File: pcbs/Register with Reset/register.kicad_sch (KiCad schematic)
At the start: 27 parts, among them U201 74HC245, U202 74HCT574, U203 74HC245

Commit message: Adding design rules
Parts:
- renumbered D201 to D301, D202 to D302, D203 to D303, D204 to D304, D205 to D305, D206 to D306, D207 to D307, D208 to D308, R201 to R301, R202 to R302, R203 to R303, R204 to R304, R205 to R305, R206 to R306, R207 to R307, R208 to R308, R209 to R309, R210 to R310, R211 to R311, R212 to R312, R213 to R313, R214 to R314, R215 to R315, R216 to R316, U201 to U301, U202 to U302, U203 to U303
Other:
- title: (none) -> 16-bit Register with Reset
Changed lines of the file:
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@@
 	(generator_version "8.0")
 	(paper "A4")
+	(title_block
+		(title "16-bit Register with Reset")
+		(rev "0")
+	)
 	(junction
 		(at 207.01 57.15)
@@
 	(label "Out4"
 		(at 264.16 52.07 0)
+		(fields_autoplaced yes)
 		(effects
 			(font
@@
 	(label "Out0"
 		(at 264.16 41.91 0)
+		(fields_autoplaced yes)
 		(effects
 			(font
@@
 	(label "In2"
 		(at 27.94 46.99 0)
+		(fields_autoplaced yes)
 		(effects
 			(font
@@
 	(label "Out6"
 		(at 264.16 57.15 0)
+		(fields_autoplaced yes)
 		(effects
 			(font
@@
 	(label "In5"
 		(at 27.94 54.61 0)
+		(fields_autoplaced yes)
 		(effects
 			(font
@@
 	(label "In7"
 		(at 27.94 59.69 0)
+		(fields_autoplaced yes)
 		(effects
 			(font
@@
 	(label "In6"
 		(at 27.94 57.15 0)
+		(fields_autoplaced yes)
 		(effects
 			(font
@@
 	(label "Out2"
 		(at 264.16 46.99 0)
+		(fields_autoplaced yes)
 		(effects
 			(font
@@
 	(label "In0"
 		(at 27.94 41.91 0)
+		(fields_autoplaced yes)
 		(effects
 			(font
@@
 	(label "Out7"
 		(at 264.16 59.69 0)
+		(fields_autoplaced yes)
 		(effects
 			(font
@@
 	(label "In1"
 		(at 27.94 44.45 0)
+		(fields_autoplaced yes)
 		(effects
 			(font
@@
 	(label "Out5"
 		(at 264.16 54.61 0)
+		(fields_autoplaced yes)
 		(effects
 			(font
@@
 	(label "Out3"
 		(at 264.16 49.53 0)
+		(fields_autoplaced yes)
 		(effects
 			(font
@@
 	(label "Out1"
 		(at 264.16 44.45 0)
+		(fields_autoplaced yes)
 		(effects
 			(font
@@
 	(label "In3"
 		(at 27.94 49.53 0)
+		(fields_autoplaced yes)
 		(effects
 			(font
@@
 	(label "In4"
 		(at 27.94 52.07 0)
+		(fields_autoplaced yes)
 		(effects
 			(font
@@
 		(dnp no)
 		(fields_autoplaced yes)
-		(property "Reference" "R214"
+		(property "Reference" "R314"
 			(at 199.39 93.9799 0)
 			(effects
@@
 		(dnp no)
 		(fields_autoplaced yes)
-		(property "Reference" "U202"
+		(property "Reference" "U302"
 			(at 134.2741 34.29 0)
 			(effects
@@
 		(dnp no)
 		(fields_autoplaced yes)
-		(property "Reference" "R204"
+		(property "Reference" "R304"
 			(at 80.01 67.3099 0)
 			(effects
@@
 		(dnp no)
 		(fields_autoplaced yes)
-		(property "Reference" "D203"
+		(property "Reference" "D303"
 			(at 170.18 80.3274 90)
 			(effects
@@
 		(dnp no)
 		(fields_autoplaced yes)
-		(property "Reference" "#PWR0212"
+		(property "Reference" "#PWR0312"
 			(at 251.46 87.63 0)
 			(effects
@@
 		(dnp no)
 		(fields_autoplaced yes)
-		(property "Reference" "#PWR0211"
+		(property "Reference" "#PWR0311"
 			(at 251.46 33.02 0)
 			(effects
@@
 		(dnp no)
 		(fields_autoplaced yes)
-		(property "Reference" "R216"
+		(property "Reference" "R316"
 			(at 219.71 93.9799 0)
 			(effects
@@
 		(dnp no)
 		(fields_autoplaced yes)
-		(property "Reference" "D205"
+		(property "Reference" "D305"
 			(at 190.5 80.3274 90)
 			(effects
@@
 		(dnp no)
 		(fields_autoplaced yes)
-		(property "Reference" "R206"
+		(property "Reference" "R306"
 			(at 88.9 67.3099 0)
 			(effects
@@
 		(dnp no)
 		(fields_autoplaced yes)
-		(property "Reference" "#PWR0203"
+		(property "Reference" "#PWR0303"
 			(at 50.8 87.63 0)
 			(effects
@@
 		(dnp no)
 		(fields_autoplaced yes)
-		(property "Reference" "R210"
+		(property "Reference" "R310"
 			(at 158.75 93.9799 0)
 			(effects
@@
 		(dnp no)
 		(fields_autoplaced yes)
-		(property "Reference" "#PWR0208"
+		(property "Reference" "#PWR0308"
 			(at 132.08 87.63 0)
 			(effects
@@
 		(dnp no)
 		(fields_autoplaced yes)
-		(property "Reference" "R209"
+		(property "Reference" "R309"
 			(at 149.86 93.9799 0)
 			(effects
@@
 		(dnp no)
 		(fields_autoplaced yes)
-		(property "Reference" "#PWR0205"
+		(property "Reference" "#PWR0305"
 			(at 68.58 85.09 0)
 			(effects
@@
 		(dnp no)
 		(fields_autoplaced yes)
-		(property "Reference" "R211"
+		(property "Reference" "R311"
 			(at 168.91 93.9799 0)
 			(effects
@@
 		(dnp no)
 		(fields_autoplaced yes)
-		(property "Reference" "R202"
+		(property "Reference" "R302"
 			(at 71.12 67.3099 0)
 			(effects
@@
 		(dnp no)
 		(fields_autoplaced yes)
-		(property "Reference" "R203"
+		(property "Reference" "R303"
 			(at 80.01 33.0199 0)
 			(effects
@@
 		(dnp no)
 		(fields_autoplaced yes)
-		(property "Reference" "D204"
+		(property "Reference" "D304"
 			(at 180.34 80.3274 90)
 			(effects
@@
 		(dnp no)
 		(fields_autoplaced yes)
-		(property "Reference" "#PWR0202"
+		(property "Reference" "#PWR0302"
 			(at 50.8 34.29 0)
 			(effects
@@
 		(dnp no)
 		(fields_autoplaced yes)
-		(property "Reference" "#PWR0207"
+		(property "Reference" "#PWR0307"
 			(at 132.08 35.56 0)
 			(effects
@@
 		(dnp no)
 		(fields_autoplaced yes)
-		(property "Reference" "R212"
+		(property "Reference" "R312"
 			(at 179.07 93.9799 0)
 			(effects
@@
 		(dnp no)
 		(fields_autoplaced yes)
-		(property "Reference" "R207"
+		(property "Reference" "R307"
 			(at 97.79 33.0199 0)
 			(effects
@@
 		(dnp no)
 		(fields_autoplaced yes)
-		(property "Reference" "#PWR0206"
+		(property "Reference" "#PWR0306"
 			(at 106.68 67.31 0)
 			(effects
@@
 		(dnp no)
 		(fields_autoplaced yes)
-		(property "Reference" "R213"
+		(property "Reference" "R313"
 			(at 189.23 93.9799 0)
 			(effects
@@
 		(dnp no)
 		(fields_autoplaced yes)
-		(property "Reference" "U203"
+		(property "Reference" "U303"
 			(at 253.6541 34.29 0)
 			(effects
@@
 		(dnp no)
 		(fields_autoplaced yes)
-		(property "Reference" "R215"
+		(property "Reference" "R315"
 			(at 209.55 93.9799 0)
 			(effects
@@
 		(dnp no)
 		(fields_autoplaced yes)
-		(property "Reference" "R205"
+		(property "Reference" "R305"
 			(at 88.9 33.0199 0)
 			(effects
@@
 		(dnp no)
 		(fields_autoplaced yes)
-		(property "Reference" "#PWR0210"
+		(property "Reference" "#PWR0310"
 			(at 236.22 64.77 0)
 			(effects
@@
 		(dnp no)
 		(fields_autoplaced yes)
-		(property "Reference" "D206"
+		(property "Reference" "D306"
 			(at 200.66 80.3274 90)
 			(effects
@@
 		(dnp no)
 		(fields_autoplaced yes)
-		(property "Reference" "#PWR0204"
+		(property "Reference" "#PWR0304"
 			(at 68.58 19.05 0)
 			(effects
@@
 		(dnp no)
 		(fields_autoplaced yes)
-		(property "Reference" "R201"
+		(property "Reference" "R301"
 			(at 71.12 33.0199 0)
 			(effects
@@
 		(dnp no)
 		(fields_autoplaced yes)
-		(property "Reference" "#PWR0201"
+		(property "Reference" "#PWR0301"
 			(at 35.56 64.77 0)
 			(effects
@@
 		(dnp no)
 		(fields_autoplaced yes)
-		(property "Reference" "#PWR0209"
+		(property "Reference" "#PWR0309"
 			(at 147.32 110.49 0)
 			(effects
@@
 		(dnp no)
 		(fields_autoplaced yes)
-		(property "Reference" "D208"
+		(property "Reference" "D308"
 			(at 220.98 80.3274 90)
 			(effects
@@
 		(dnp no)
 		(fields_autoplaced yes)
-		(property "Reference" "D207"
+		(property "Reference" "D307"
 			(at 210.82 80.3274 90)
 			(effects
@@
 		(dnp no)
 		(fields_autoplaced yes)
-		(property "Reference" "D202"
+		(property "Reference" "D302"
 			(at 160.02 80.3274 90)
 			(effects
@@
 		(dnp no)
 		(fields_autoplaced yes)
-		(property "Reference" "U201"
+		(property "Reference" "U301"
 			(at 52.9941 34.29 0)
 			(effects
@@
 		(dnp no)
 		(fields_autoplaced yes)
-		(property "Reference" "R208"
+		(property "Reference" "R308"
 			(at 97.79 67.3099 0)
 			(effects
@@
 		(dnp no)
 		(fields_autoplaced yes)
-		(property "Reference" "D201"
+		(property "Reference" "D301"
 			(at 151.13 80.3274 90)
 			(effects

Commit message: Routing the actual registers
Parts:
- added C201: C, Capacitor_SMD:C_0603_1608Metric, symbol Device:C
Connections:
- net +5V: now also C201.1; no longer U303.1 (A->B)
- net GND: now also U303.1 (A->B), C201.2
- net Out0: now also U303.9 (A7); no longer U303.18 (B0)
- net Out1: now also U303.8 (A6); no longer U303.17 (B1)
- net Out2: now also U303.7 (A5); no longer U303.16 (B2)
- net Out3: now also U303.6 (A4); no longer U303.15 (B3)
- net Out4: now also U303.5 (A3); no longer U303.14 (B4)
- net Out5: now also U303.4 (A2); no longer U303.13 (B5)
- net Out6: now also U303.3 (A1); no longer U303.12 (B6)
- net Out7: now also U303.2 (A0); no longer U303.11 (B7)
- net RegClk: now reaches U302.11 (Cp)
- net at D308.2 (A), U302.12 (Q7): now also U303.18 (B0); no longer U303.9 (A7)
- net at D307.2 (A), U302.13 (Q6): now also U303.17 (B1); no longer U303.8 (A6)
- net at D306.2 (A), U302.14 (Q5): now also U303.16 (B2); no longer U303.7 (A5)
- net at D305.2 (A), U302.15 (Q4): now also U303.15 (B3); no longer U303.6 (A4)
- net at D304.2 (A), U302.16 (Q3): now also U303.14 (B4); no longer U303.5 (A3)
- net at D303.2 (A), U302.17 (Q2): now also U303.13 (B5); no longer U303.4 (A2)
- net at D302.2 (A), U302.18 (Q1): now also U303.12 (B6); no longer U303.3 (A1)
- net at D301.2 (A), U302.19 (Q0): now also U303.11 (B7); no longer U303.2 (A0)
- net at U301.17 (B1), U302.3 (D1): now also R302.1; no longer R303.2
- net at U301.16 (B2), U302.4 (D2): now also R303.2; no longer R305.2
- net at U301.15 (B3), U302.5 (D3): now also R304.1; no longer R307.2
- net at U301.14 (B4), U302.6 (D4): now also R305.2; no longer R302.1
- net at U301.13 (B5), U302.7 (D5): now also R306.1; no longer R304.1
- net at U301.12 (B6), U302.8 (D6): now also R307.2; no longer R306.1
- net ~{OE}: now reaches U303.19 (CE)
- net ~{ZeroInput}: now reaches U301.19 (CE)
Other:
- moved on the sheet: U303

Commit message: Working on reset logic and some routing
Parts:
- renumbered C201 to C301
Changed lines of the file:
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@@
 		(dnp no)
 		(fields_autoplaced yes)
-		(property "Reference" "C201"
+		(property "Reference" "C301"
 			(at 132.08 132.0799 0)
 			(effects
@@
 		(dnp no)
 		(fields_autoplaced yes)
-		(property "Reference" "#PWR0213"
+		(property "Reference" "#PWR0313"
 			(at 128.27 146.05 0)
 			(effects
@@
 		(dnp no)
 		(fields_autoplaced yes)
-		(property "Reference" "#PWR0214"
+		(property "Reference" "#PWR0314"
 			(at 128.27 129.54 0)
 			(effects

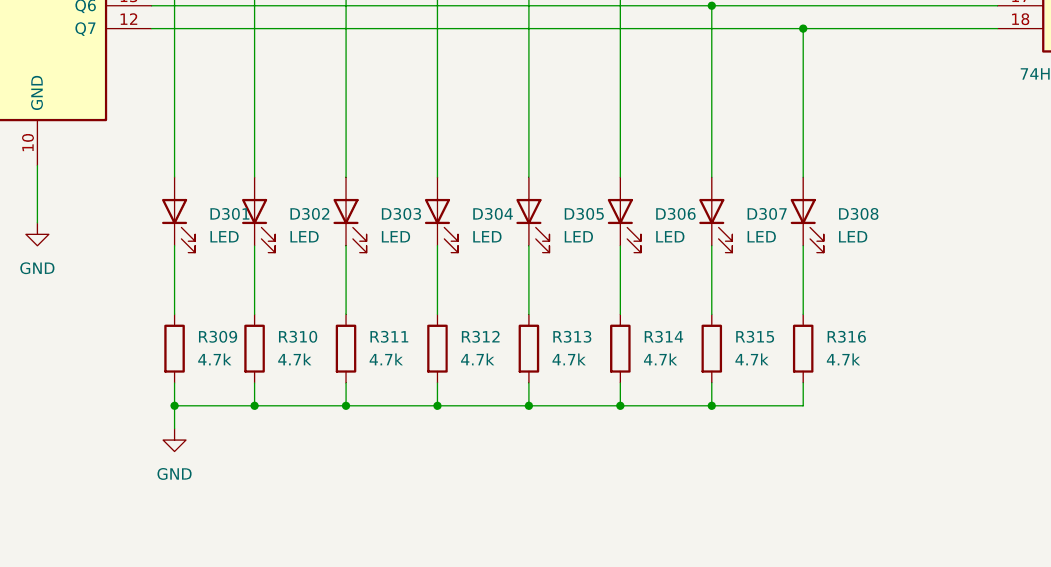
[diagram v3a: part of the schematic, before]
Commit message: First draft of whole board
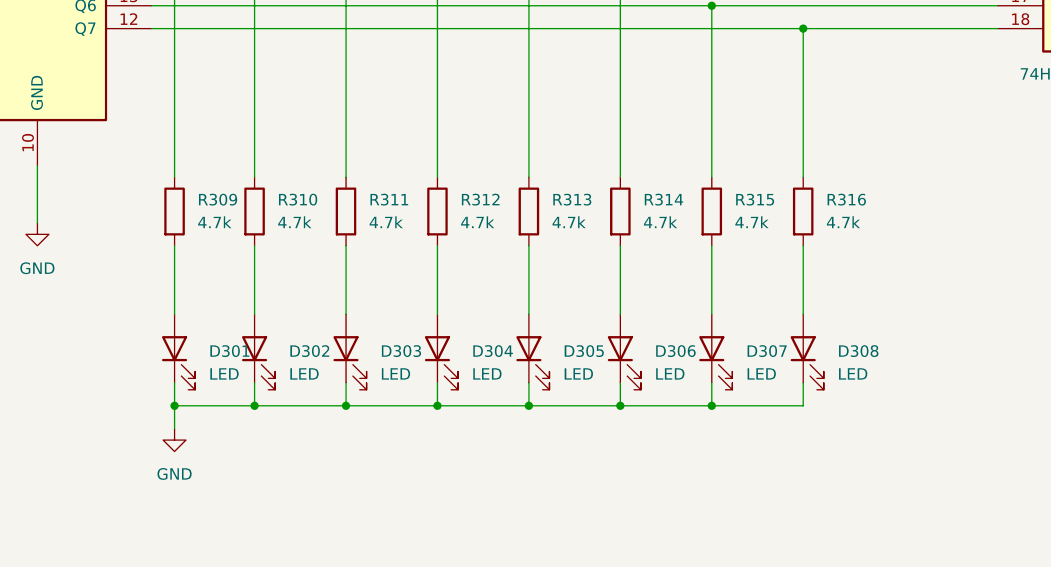
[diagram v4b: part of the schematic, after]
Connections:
- net GND: now also D301.1 (K), D302.1 (K), D303.1 (K), D304.1 (K), D305.1 (K), D306.1 (K), D307.1 (K), D308.1 (K); no longer R309.2, R310.2, R311.2, R312.2, R313.2, R314.2, R315.2, R316.2
- net at R314.1: now also U302.14 (Q5), U303.16 (B2); no longer D306.1 (K)
- net at U302.12 (Q7), U303.18 (B0): now also R316.1; no longer D308.2 (A)
- net at U302.13 (Q6), U303.17 (B1): now also R315.1; no longer D307.2 (A)
- net at U302.15 (Q4), U303.15 (B3): now also R313.1; no longer D305.2 (A)
- net at U302.16 (Q3), U303.14 (B4): now also R312.1; no longer D304.2 (A)
- net at U302.17 (Q2), U303.13 (B5): now also R311.1; no longer D303.2 (A)
- net at U302.18 (Q1), U303.12 (B6): now also R310.1; no longer D302.2 (A)
- net at U302.19 (Q0), U303.11 (B7): now also R309.1; no longer D301.2 (A)
- new net: D306.2 (A), R314.2
- new net: D303.2 (A), R311.2
- new net: D308.2 (A), R316.2
- new net: D305.2 (A), R313.2
- new net: D302.2 (A), R310.2
- new net: D301.2 (A), R309.2
- new net: D304.2 (A), R312.2
- new net: D307.2 (A), R315.2
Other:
- moved on the sheet: D301, D302, D303, D304, D305, D306, D307, D308, R309, R310, R311, R312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

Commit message: Fix the reset logic....
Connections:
- net ~{ZeroInput} renamed ZeroInput
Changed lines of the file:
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@@
 		)
 	)
-	(hierarchical_label "~{ZeroInput}"
+	(hierarchical_label "ZeroInput"
 		(shape input)
 		(at 26.67 67.31 180)

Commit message: Get buses routed
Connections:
- net Out0: now also U303.2 (A0); no longer U303.9 (A7)
- net Out1: now also U303.3 (A1); no longer U303.8 (A6)
- net Out2: now also U303.4 (A2); no longer U303.7 (A5)
- net Out3: now also U303.5 (A3); no longer U303.6 (A4)
- net Out4: now also U303.6 (A4); no longer U303.5 (A3)
- net Out5: now also U303.7 (A5); no longer U303.4 (A2)
- net Out6: now also U303.8 (A6); no longer U303.3 (A1)
- net Out7: now also U303.9 (A7); no longer U303.2 (A0)
- net at R314.1, U302.14 (Q5): now also U303.13 (B5); no longer U303.16 (B2)
- net at R316.1, U302.12 (Q7): now also U303.11 (B7); no longer U303.18 (B0)
- net at R315.1, U302.13 (Q6): now also U303.12 (B6); no longer U303.17 (B1)
- net at R313.1, U302.15 (Q4): now also U303.14 (B4); no longer U303.15 (B3)
- net at R312.1, U302.16 (Q3): now also U303.15 (B3); no longer U303.14 (B4)
- net at R311.1, U302.17 (Q2): now also U303.16 (B2); no longer U303.13 (B5)
- net at R310.1, U302.18 (Q1): now also U303.17 (B1); no longer U303.12 (B6)
- net at R309.1, U302.19 (Q0): now also U303.18 (B0); no longer U303.11 (B7)
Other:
- moved on the sheet: U303
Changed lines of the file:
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@@
 	(wire
 		(pts
-			(xy 264.16 34.29) (xy 269.24 34.29)
+			(xy 264.16 67.31) (xy 269.24 67.31)
 		)
 		(stroke
@@
 	(wire
 		(pts
-			(xy 251.46 22.86) (xy 251.46 26.67)
+			(xy 251.46 78.74) (xy 251.46 74.93)
 		)
 		(stroke
@@
 	(wire
 		(pts
-			(xy 251.46 67.31) (xy 251.46 71.12)
+			(xy 251.46 34.29) (xy 251.46 30.48)
 		)
 		(stroke
@@
 	(wire
 		(pts
-			(xy 264.16 36.83) (xy 267.97 36.83)
+			(xy 264.16 64.77) (xy 267.97 64.77)
 		)
 		(stroke
@@
 	(hierarchical_label "~{OE}"
 		(shape input)
-		(at 269.24 34.29 0)
+		(at 269.24 67.31 0)
 		(fields_autoplaced yes)
 		(effects
@@
 	(symbol
 		(lib_id "power:GND")
-		(at 251.46 22.86 180)
+		(at 251.46 78.74 0)
 		(unit 1)
 		(exclude_from_sim no)
@@
 		(fields_autoplaced yes)
 		(property "Reference" "#PWR0312"
-			(at 251.46 16.51 0)
+			(at 251.46 85.09 0)
 			(effects
 				(font
@@
 		)
 		(property "Value" "GND"
-			(at 251.46 17.78 0)
+			(at 251.46 83.82 0)
 			(effects
 				(font
@@
 		)
 		(property "Footprint" ""
-			(at 251.46 22.86 0)
+			(at 251.46 78.74 0)
 			(effects
 				(font
@@
 		)
 		(property "Datasheet" ""
-			(at 251.46 22.86 0)
+			(at 251.46 78.74 0)
 			(effects
 				(font
@@
 		)
 		(property "Description" "Power symbol creates a global label with name \"GND\" , ground"
-			(at 251.46 22.86 0)
+			(at 251.46 78.74 0)
 			(effects
 				(font
@@
 	(symbol
 		(lib_id "power:+5V")
-		(at 251.46 71.12 180)
+		(at 251.46 30.48 0)
 		(unit 1)
 		(exclude_from_sim no)
@@
 		(fields_autoplaced yes)
 		(property "Reference" "#PWR0311"
-			(at 251.46 67.31 0)
+			(at 251.46 34.29 0)
 			(effects
 				(font
@@
 		)
 		(property "Value" "+5V"
-			(at 251.46 76.2 0)
+			(at 251.46 25.4 0)
 			(effects
 				(font
@@
 		)
 		(property "Footprint" ""
-			(at 251.46 71.12 0)
+			(at 251.46 30.48 0)
 			(effects
 				(font
@@
 		)
 		(property "Datasheet" ""
-			(at 251.46 71.12 0)
+			(at 251.46 30.48 0)
 			(effects
 				(font
@@
 		)
 		(property "Description" "Power symbol creates a global label with name \"+5V\""
-			(at 251.46 71.12 0)
+			(at 251.46 30.48 0)
 			(effects
 				(font
@@
 	(symbol
 		(lib_id "power:GND")
-		(at 267.97 36.83 90)
+		(at 267.97 64.77 90)
 		(unit 1)
 		(exclude_from_sim no)
@@
 		(fields_autoplaced yes)
 		(property "Reference" "#PWR0310"
-			(at 274.32 36.83 0)
+			(at 274.32 64.77 0)
 			(effects
 				(font
@@
 		)
 		(property "Value" "GND"
-			(at 271.78 36.8299 90)
+			(at 271.78 64.7699 90)
 			(effects
 				(font
@@
 		)
 		(property "Footprint" ""
-			(at 267.97 36.83 0)
+			(at 267.97 64.77 0)
 			(effects
 				(font
@@
 		)
 		(property "Datasheet" ""
-			(at 267.97 36.83 0)
+			(at 267.97 64.77 0)
 			(effects
 				(font
@@
 		)
 		(property "Description" "Power symbol creates a global label with name \"GND\" , ground"
-			(at 267.97 36.83 0)
+			(at 267.97 64.77 0)
 			(effects
 				(font
@@
 	(symbol
 		(lib_id "74xx:74HC245")
-		(at 251.46 46.99 180)
+		(at 251.46 54.61 0)
+		(mirror y)
 		(unit 1)
 		(exclude_from_sim no)
@@
 		(dnp no)
 		(property "Reference" "U303"
-			(at 249.2659 67.31 0)
+			(at 249.2659 34.29 0)
 			(effects
 				(font
@@
 		)
 		(property "Value" "74HC245"
-			(at 249.2659 64.77 0)
+			(at 249.2659 36.83 0)
 			(effects
 				(font
@@
 		)
 		(property "Footprint" "Package_SO:SOIC-20W_7.5x12.8mm_P1.27mm"
-			(at 251.46 46.99 0)
+			(at 251.46 54.61 0)
 			(effects
 				(font
@@
 		)
 		(property "Datasheet" "http://www.ti.com/lit/gpn/sn74HC245"
-			(at 251.46 46.99 0)
+			(at 251.46 54.61 0)
 			(effects
 				(font
@@
 		)
 		(property "Description" "Octal BUS Transceivers, 3-State outputs"
-			(at 251.46 46.99 0)
+			(at 251.46 54.61 0)
 			(effects
 				(font
@@
 		)
 		(property "LCSC" "C5625"
-			(at 251.46 46.99 0)
+			(at 251.46 54.61 0)
 			(effects
 				(font
